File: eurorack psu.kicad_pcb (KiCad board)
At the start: 2 copper layers, 100 x 60 mm, 30 parts, among them J1 Screw Terminal 1x3, J2 Screw_Terminal_01x03, M3 MountingHole_3.2mm_M3_DIN965_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, U1 LM7812, U2 LM7912

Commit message: added control LEDs
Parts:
- removed the svg2mod at (149.3, 60.6)
- removed the svg2mod at (149.1, 84.4)
- added D7: LED, LED_THT:LED_D3.0mm, F.Cu at (149.2, 64.0)
- added D8: LED, LED_THT:LED_D3.0mm, F.Cu at (151.5, 87.8)
- added R3: R, Resistor_THT:R_Axial_DIN0207_L6.3mm_D2.5mm_P7.62mm_Horizontal, F.Cu at (141.9, 57.2)
- added R4: R, Resistor_THT:R_Axial_DIN0207_L6.3mm_D2.5mm_P7.62mm_Horizontal, F.Cu at (142.2, 95.2)
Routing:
- net Net-(D8-Pad1): track 0.00 -> 8.22 mm
- net Net-(D7-Pad2): track 0.00 -> 7.78 mm

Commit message: added PWR_FLAG to clear ERC errors
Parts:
- U1: value LM7812 -> LM7812_TO220
- U2: value LM7912 -> LM7912_TO220

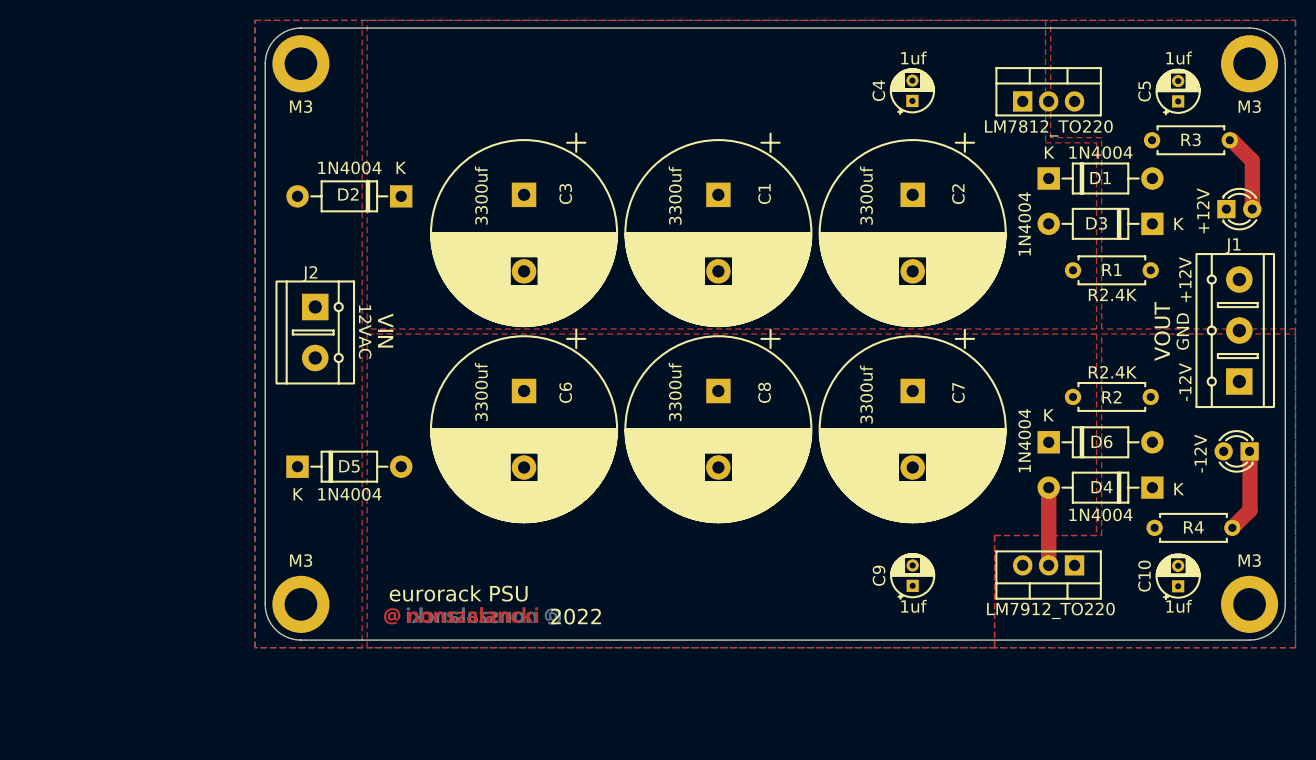
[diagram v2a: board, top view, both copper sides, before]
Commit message: updated to full bridge
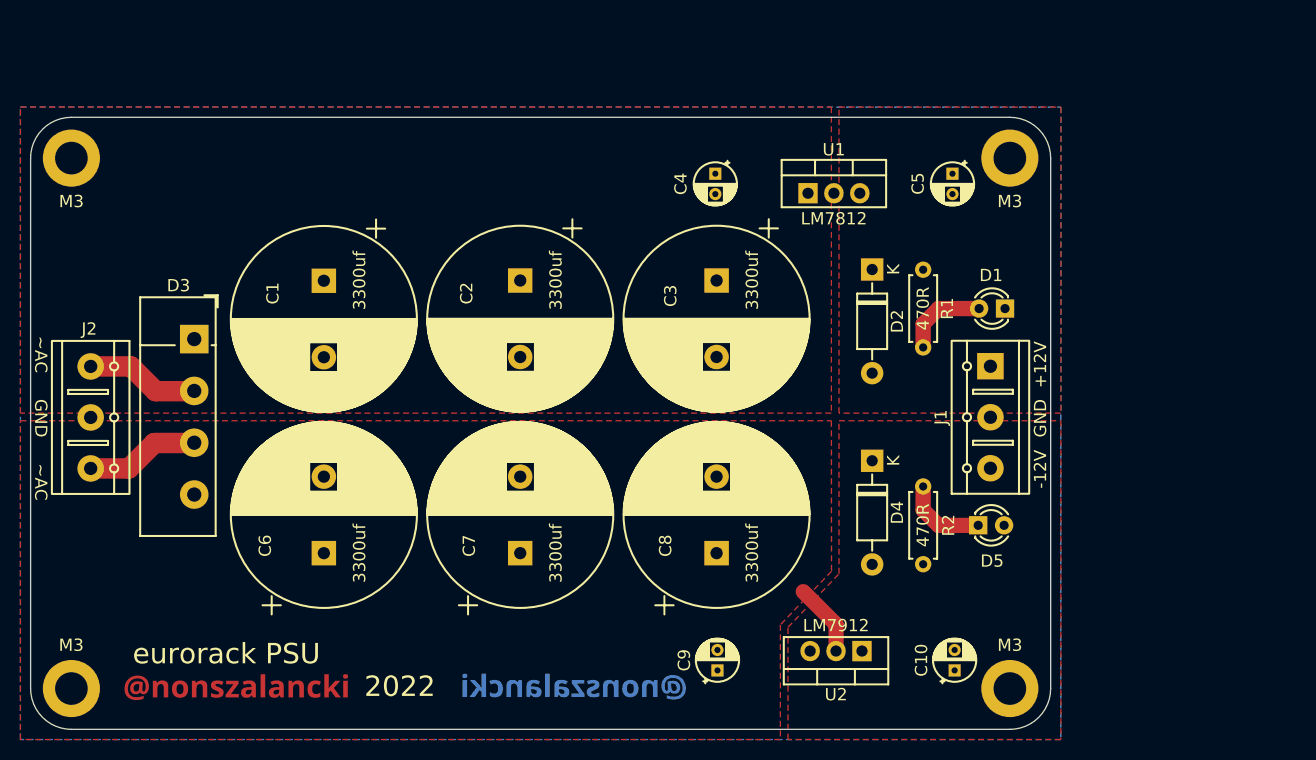
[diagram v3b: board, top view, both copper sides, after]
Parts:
- removed D6: 1N4004, Diode_THT:D_DO-41_SOD81_P10.16mm_Horizontal
- removed D7, D8: LED, LED_THT:LED_D3.0mm
- removed the M3 at (58.5, 102.8)
- removed the M3 at (151.5, 49.8)
- removed the M3 at (151.5, 102.8)
- removed the M3 at (58.5, 49.8)
- removed R3, R4: R, Resistor_THT:R_Axial_DIN0207_L6.3mm_D2.5mm_P7.62mm_Horizontal
- removed the svg2mod at (66.6, 103.0)
- removed the svg2mod at (84.0, 103.1)
- added M3: MountingHole_3.2mm_M3_DIN965_Pad, MountingHole:MountingHole_3.2mm_M3_DIN965_Pad, F.Cu at (36.0, 111.0)
- added M3: MountingHole_3.2mm_M3_DIN965_Pad, MountingHole:MountingHole_3.2mm_M3_DIN965_Pad, F.Cu at (36.0, 59.0)
- added M3: MountingHole_3.2mm_M3_DIN965_Pad, MountingHole:MountingHole_3.2mm_M3_DIN965_Pad, F.Cu at (128.0, 59.0)
- added M3: MountingHole_3.2mm_M3_DIN965_Pad, MountingHole:MountingHole_3.2mm_M3_DIN965_Pad, F.Cu at (128.0, 111.0)
- added svg2mod: G***, Signature:@ nonszalancki 3-sans-serif-bold-F.Cu.svg, F.Cu at (41.2, 109.6)
- added svg2mod: G***, Signature:@ nonszalancki 3-sans-serif-bold-F.Cu.svg, B.Cu at (96.2, 109.5)
- D1, D5: value 1N4004 -> LED; footprint Diode_THT:D_DO-41_SOD81_P10.16mm_Horizontal -> LED_THT:LED_D3.0mm
- D3: value 1N4004 -> KBU8M; footprint Diode_THT:D_DO-41_SOD81_P10.16mm_Horizontal -> Diode_THT:Diode_Bridge_Vishay_KBU
- J2: footprint TerminalBlock_XINYA:TerminalBlock_XINYA_XY301-1x2-P5.00mm -> TerminalBlock_XINYA:TerminalBlock_XINYA_XY301-1x3-P5.00mm
- R1, R2: value R2.4K -> 470R
- U1: value LM7812_TO220 -> LM7812
- U2: value LM7912_TO220 -> LM7912
- moved D3 94.6 mm to (48.0, 76.7), turned to -90 degrees
- moved D5 67.0 mm to (124.9, 95.0)
- moved D2 46.7 mm to (114.5, 69.9), turned to -90 degrees
- moved C7 41.6 mm to (80.0, 97.7), turned to 90 degrees
- moved C1 39.6 mm to (60.8, 71.0)
- moved C2 39.4 mm to (80.0, 71.0)
- moved R2 27.7 mm to (119.5, 98.8), turned to 90 degrees
- moved D4 27.6 mm to (114.5, 88.7), turned to -90 degrees
- moved J1 25.5 mm to (122.3, 91.9)
- moved C6 25.3 mm to (60.8, 97.7), turned to 90 degrees
- moved C10 23.4 mm to (122.6, 109.2)
- moved C5 23.2 mm to (122.4, 60.5), turned to -90 degrees
- moved U1 22.9 mm to (108.2, 62.4)
- moved J2 22.8 mm to (41.7, 76.9)
- moved U2 22.5 mm to (113.5, 107.3)
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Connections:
- C10 pad 1: GND -> -12V
- C10 pad 2: -12V -> GND
- C6 pad 1: GND -> /L1
- C6 pad 2: /L3 -> GND
- C7 pad 1: GND -> /L1
- C7 pad 2: /L3 -> GND
- C8 pad 1: GND -> /L1
- C8 pad 2: /L3 -> GND
- C9 pad 1: GND -> /L1
- C9 pad 2: /L3 -> GND
- D1 pad 1: /L2 -> GND
- D1 pad 2: +12V -> Net-(D1-Pad2)
- D2 pad 1: /L2 -> +12V
- D2 pad 2: /L1 -> GND
- D3 pad 1: +12V -> /L2
- D3 pad 2: GND -> Net-(D3-Pad2)
- D4 pad 1: -12V -> GND
- D4 pad 2: /L3 -> -12V
- D5 pad 1: /L1 -> Net-(D5-Pad1)
- D5 pad 2: /L3 -> GND
- J2 pad 1: GND -> Net-(D3-Pad2)
- J2 pad 2: /L1 -> GND
- R1 pad 2: GND -> Net-(D1-Pad2)
- R2 pad 2: GND -> Net-(D5-Pad1)
- U2 pad 2: /L3 -> /L1
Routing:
- net Net-(D3-Pad3): track 0.00 -> 11.2 mm
- net Net-(D3-Pad2): track 0.00 -> 11.2 mm
- net Net-(D1-Pad2): track 0.00 -> 8.42 mm
- net Net-(D5-Pad1): track 0.00 -> 8.33 mm
- net Net-(D8-Pad1): track 8.22 -> 0.00 mm
- net Net-(D7-Pad2): track 7.78 -> 0.00 mm
- net /L3: track 7.62 -> 0.00 mm
- net /L1: track 0.00 -> 7.13 mm
- removed copper zone on F.Cu, net /L3
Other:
- outline, holes or cut-outs redrawn
- board text removed: "VIN"
- board text removed: "VOUT"
